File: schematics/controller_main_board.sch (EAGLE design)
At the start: 17 parts, among them U1 ULN2003AN

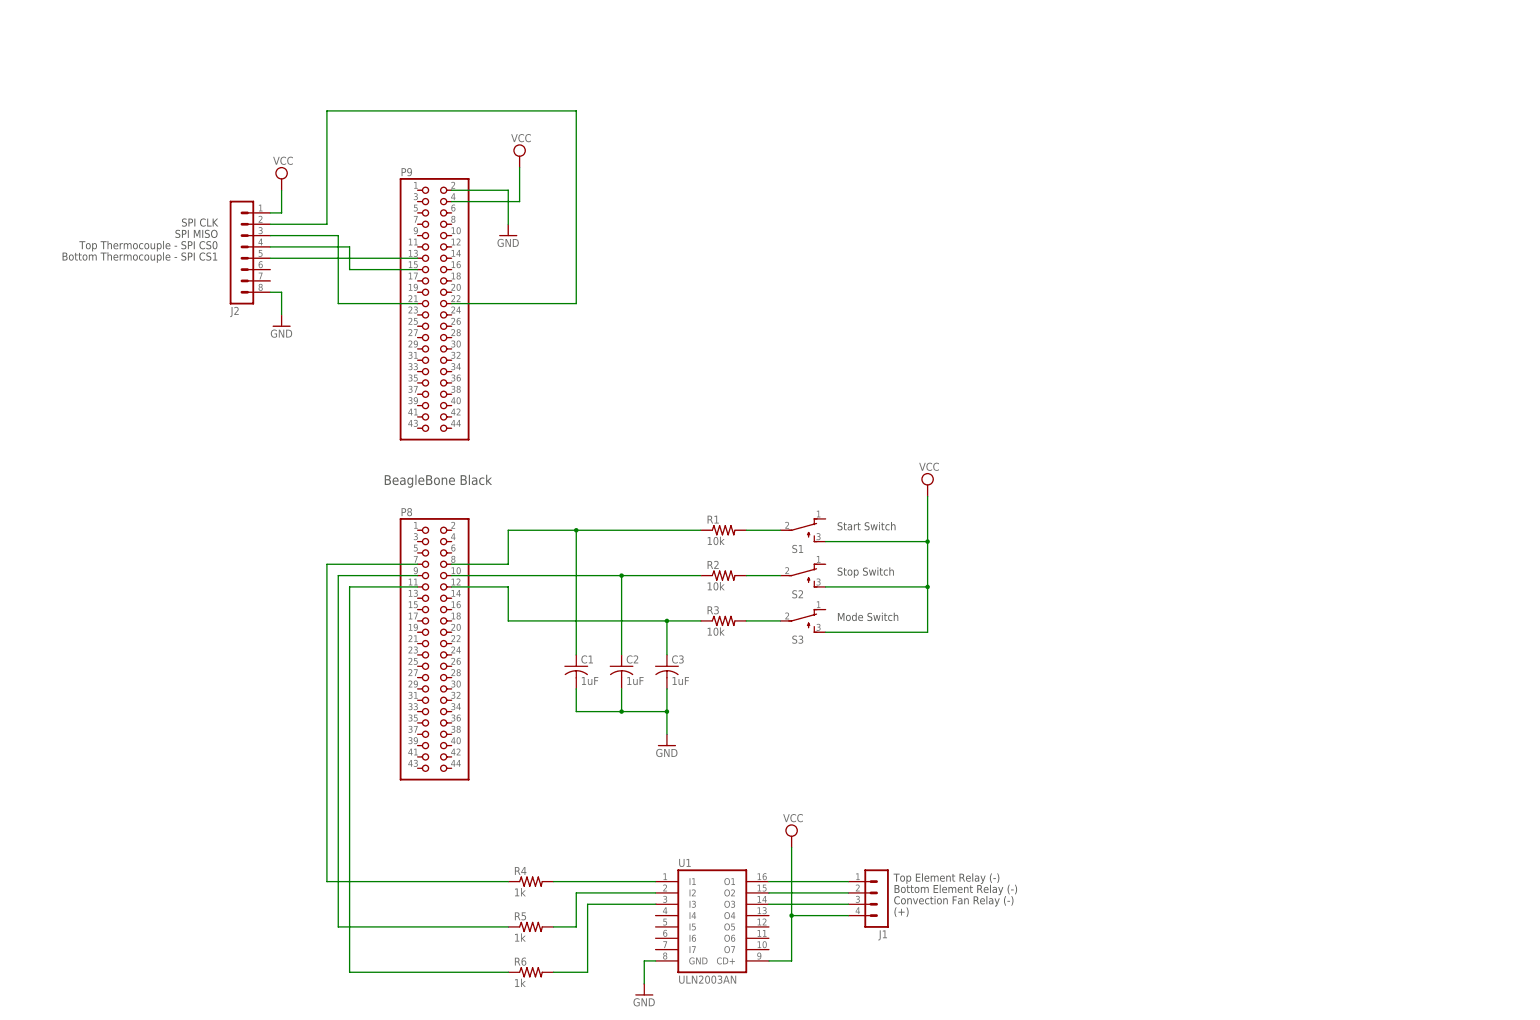
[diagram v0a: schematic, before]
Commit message: Add custom title block.
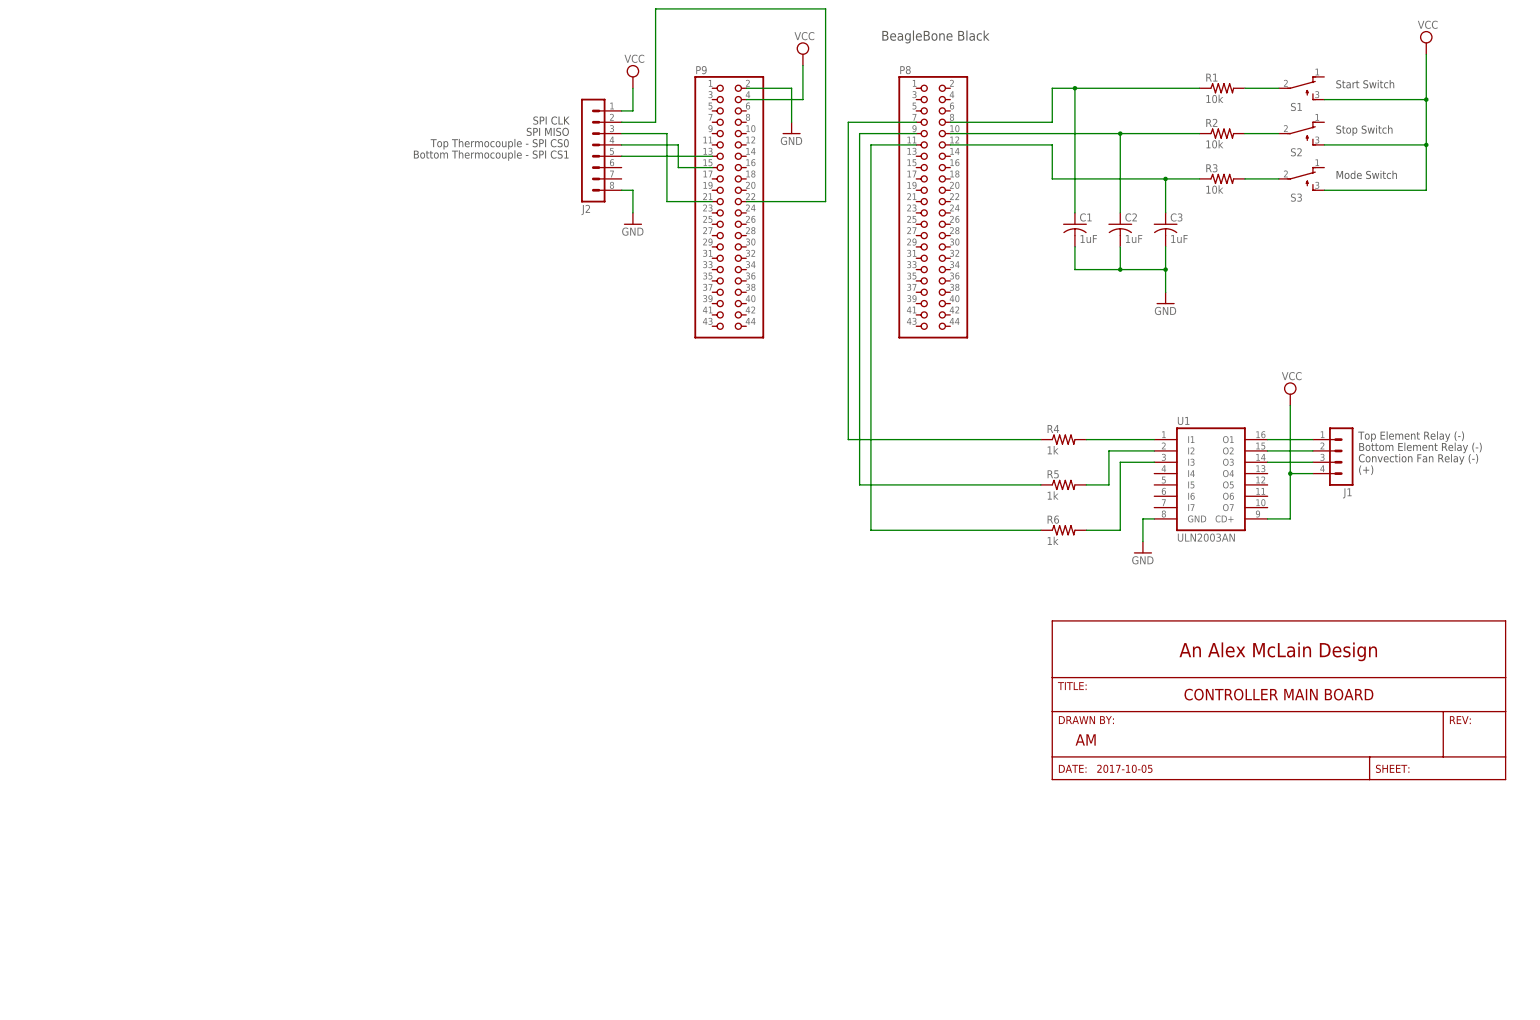
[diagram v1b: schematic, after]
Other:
- moved on the sheet: C1, C2, C3, J1, J2, P8, P9, R1, R2, R3, R4, R5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

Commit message: Add controller relays schematic.
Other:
- note added: "To Controller Relays J1"
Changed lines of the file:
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@@
 <text x="108.966" y="165.608" size="2.1844" layer="97">BeagleBone Black</text>
 <text x="215.9" y="68.58" size="1.778" layer="97">(+)</text>
+<text x="209.55" y="80.01" size="1.778" layer="97">To Controller Relays J1</text>
 </plain>
 <instances>

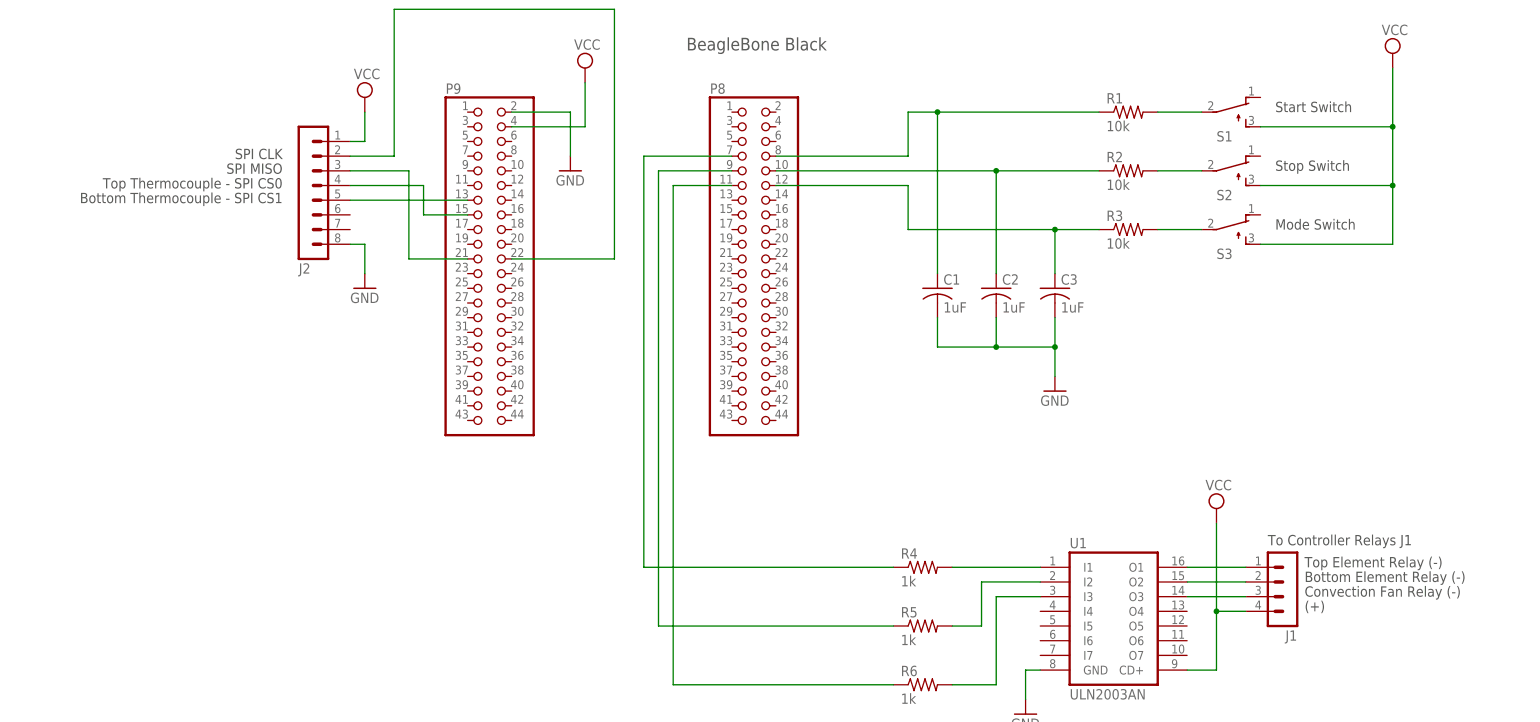
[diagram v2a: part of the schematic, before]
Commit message: Add oven thermocouples schematic.
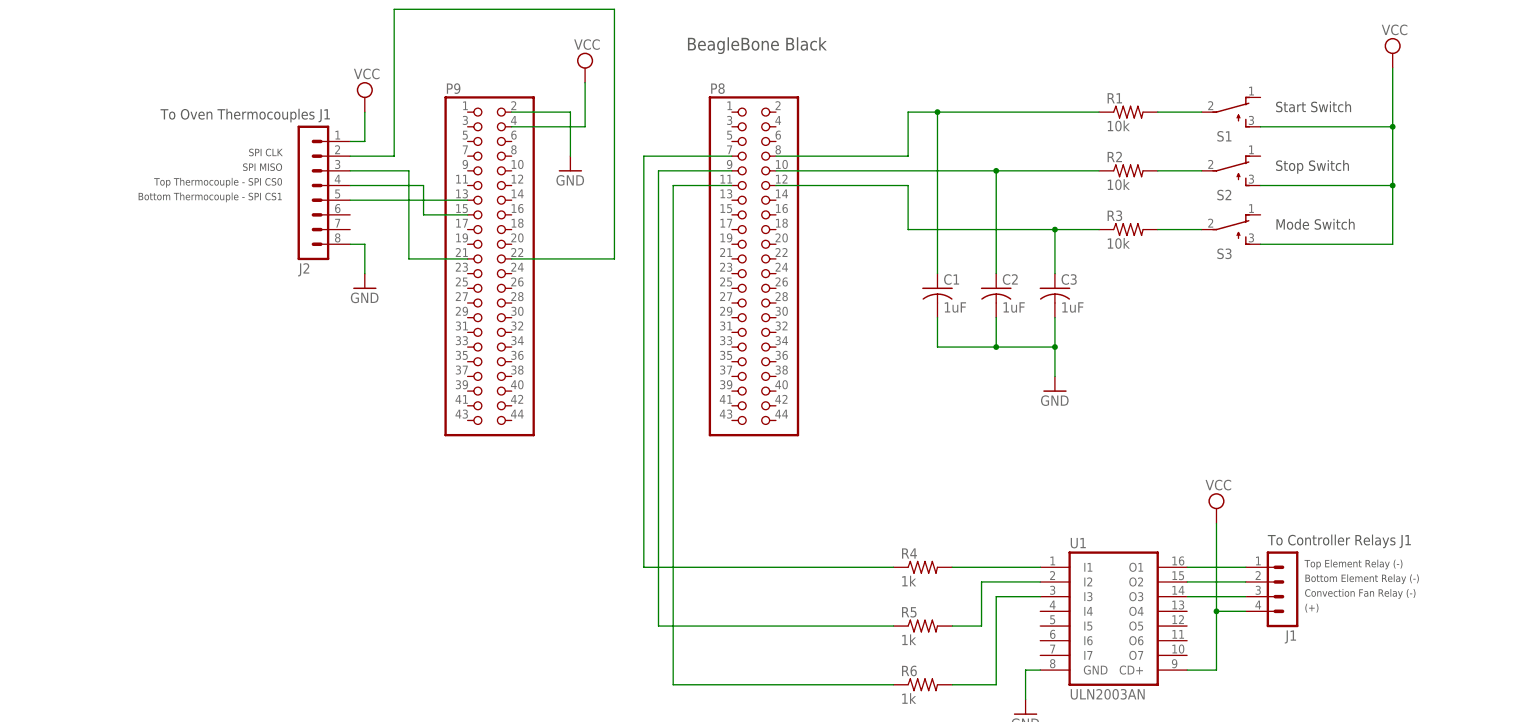
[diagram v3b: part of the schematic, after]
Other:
- note added: "To Oven Thermocouples J1"
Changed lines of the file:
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@@
 <sheet>
 <plain>
-<text x="215.9" y="76.2" size="1.778" layer="97">Top Element Relay (-)</text>
-<text x="215.9" y="73.66" size="1.778" layer="97">Bottom Element Relay (-)</text>
-<text x="215.9" y="71.12" size="1.778" layer="97">Convection Fan Relay (-)</text>
+<text x="215.9" y="76.2" size="1.27" layer="97">Top Element Relay (-)</text>
+<text x="215.9" y="73.66" size="1.27" layer="97">Bottom Element Relay (-)</text>
+<text x="215.9" y="71.12" size="1.27" layer="97">Convection Fan Relay (-)</text>
 <text x="210.82" y="154.94" size="1.778" layer="97">Start Switch</text>
 <text x="210.82" y="144.78" size="1.778" layer="97">Stop Switch</text>
 <text x="210.82" y="134.62" size="1.778" layer="97">Mode Switch</text>
-<text x="39.116" y="148.59" size="1.778" layer="97" rot="R180">SPI CLK</text>
-<text x="39.116" y="146.05" size="1.778" layer="97" rot="R180">SPI MISO</text>
-<text x="39.116" y="143.51" size="1.778" layer="97" rot="R180">Top Thermocouple - SPI CS0</text>
-<text x="39.116" y="140.97" size="1.778" layer="97" rot="R180">Bottom Thermocouple - SPI CS1</text>
+<text x="39.116" y="148.59" size="1.27" layer="97" rot="R180">SPI CLK</text>
+<text x="39.116" y="146.05" size="1.27" layer="97" rot="R180">SPI MISO</text>
+<text x="39.116" y="143.51" size="1.27" layer="97" rot="R180">Top Thermocouple - SPI CS0</text>
+<text x="39.116" y="140.97" size="1.27" layer="97" rot="R180">Bottom Thermocouple - SPI CS1</text>
 <text x="108.966" y="165.608" size="2.1844" layer="97">BeagleBone Black</text>
-<text x="215.9" y="68.58" size="1.778" layer="97">(+)</text>
+<text x="215.9" y="68.58" size="1.27" layer="97">(+)</text>
 <text x="209.55" y="80.01" size="1.778" layer="97">To Controller Relays J1</text>
+<text x="47.498" y="155.448" size="1.778" layer="97" rot="R180">To Oven Thermocouples J1</text>
 </plain>
 <instances>
